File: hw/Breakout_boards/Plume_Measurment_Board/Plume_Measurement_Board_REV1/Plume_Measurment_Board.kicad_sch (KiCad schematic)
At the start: 34 parts, among them U2 LMP7721MA/NOPB, U3 LMP2022MA/NOPB, U4 AD8475ARMZ, U5 AD8475ARMZ, U7 AD7176-2BRUZ

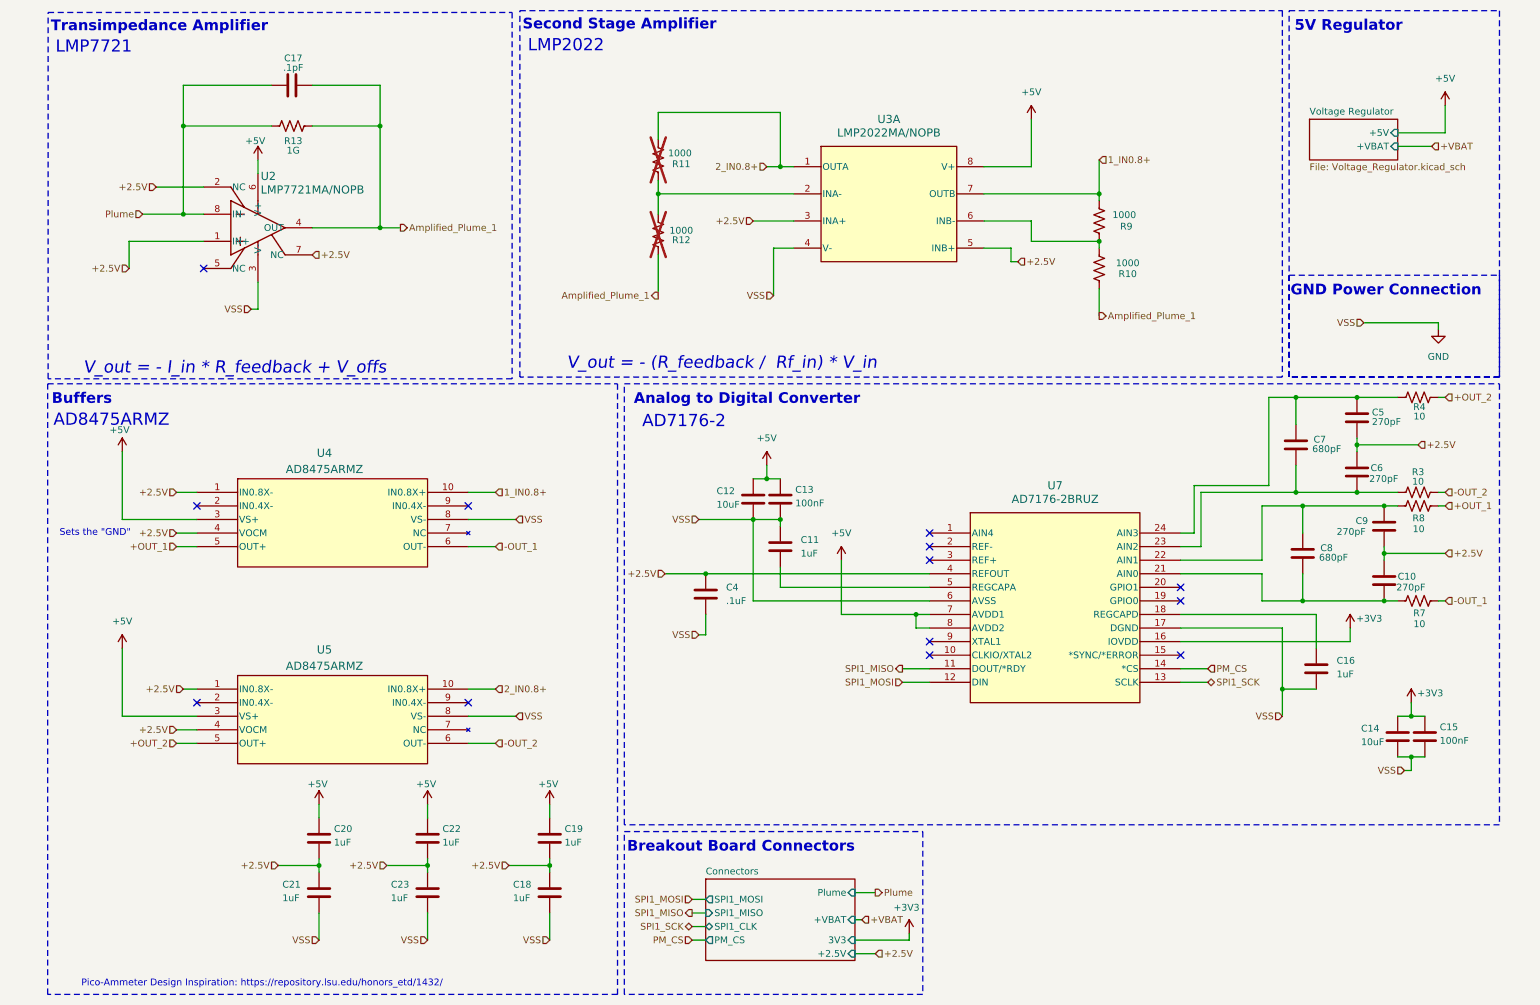
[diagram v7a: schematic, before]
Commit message: New Schematic w/ Addition of two E-spray Amplification Signals
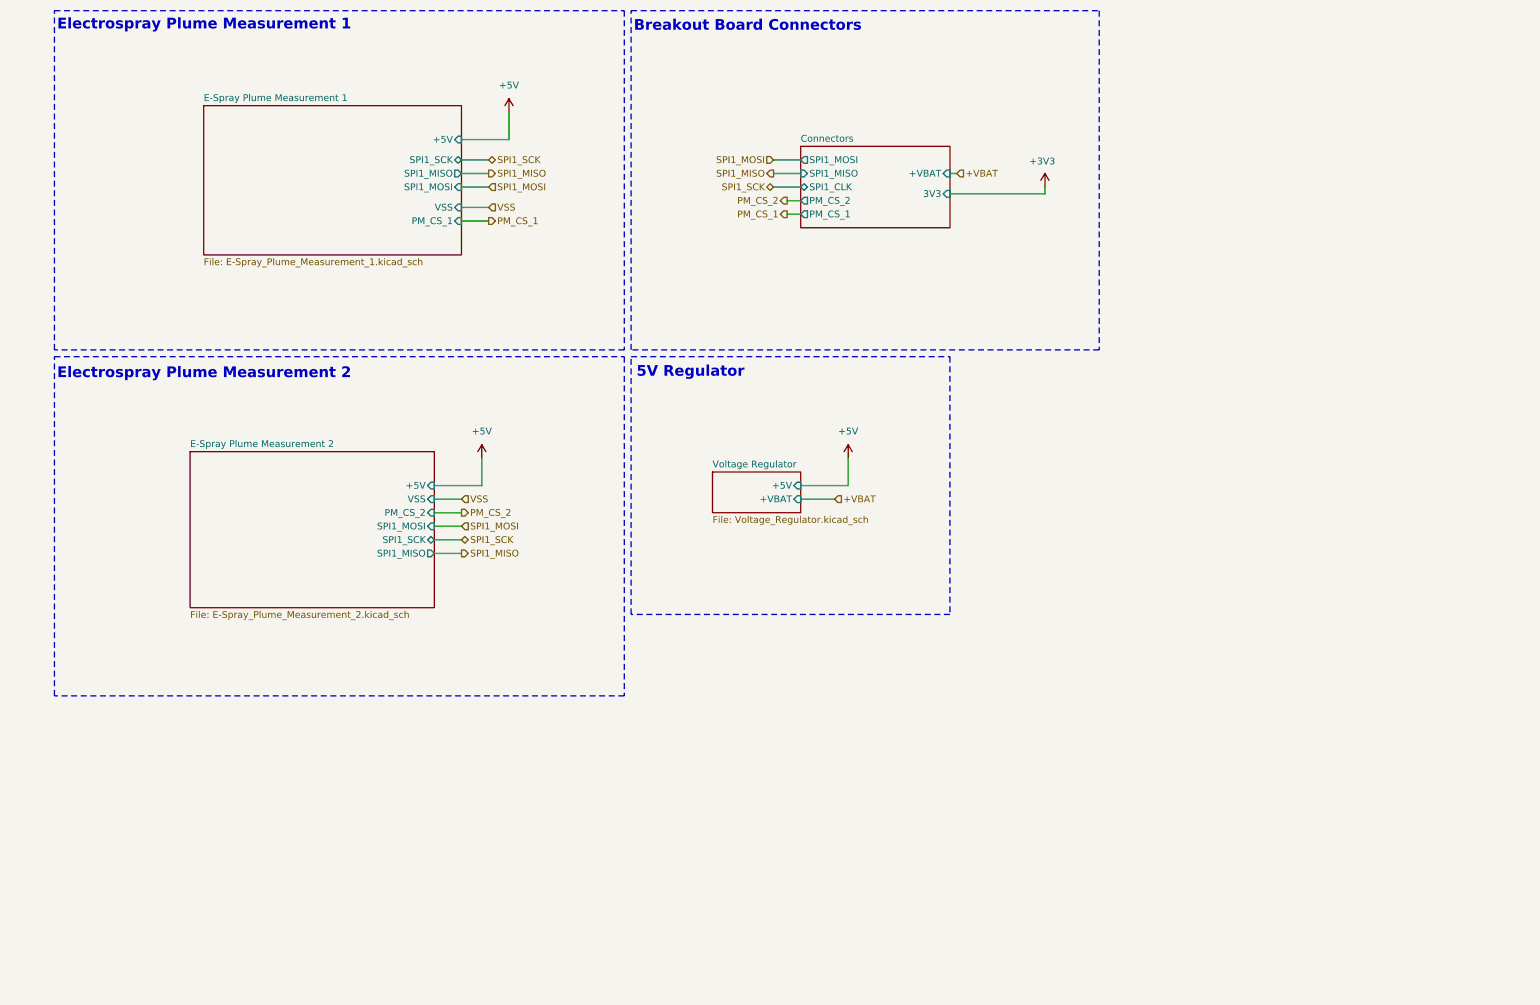
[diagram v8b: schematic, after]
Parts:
- removed C10, C5, C6, C9: 270pF, Capacitor_SMD:C_0603_1608Metric_Pad1.08x0.95mm_HandSolder, symbol Device:C
- removed C11, C19, C20, C22: 1uF, Capacitor_SMD:C_0603_1608Metric_Pad1.08x0.95mm_HandSolder, symbol Device:C
- removed C12, C14: 10uF, Capacitor_SMD:C_0805_2012Metric_Pad1.18x1.45mm_HandSolder, symbol Device:C
- removed C13, C15: 100nF, Capacitor_SMD:C_0603_1608Metric_Pad1.08x0.95mm_HandSolder, symbol Device:C
- removed C16, C18, C21, C23: 1uF, Capacitor_SMD:C_0805_2012Metric_Pad1.18x1.45mm_HandSolder, symbol Device:C
- removed C17: .1pF, Capacitor_SMD:C_0402_1005Metric_Pad0.74x0.62mm_HandSolder, symbol Device:C
- removed C4: .1uF, Capacitor_SMD:C_0603_1608Metric_Pad1.08x0.95mm_HandSolder, symbol Device:C
- removed C7, C8: 680pF, Capacitor_SMD:C_0603_1608Metric_Pad1.08x0.95mm_HandSolder, symbol Device:C
- removed R10, R11, R12, R9: 1000, Resistor_SMD:R_0603_1608Metric_Pad0.98x0.95mm_HandSolder, symbol Device:R_US
- removed R13: 1G, Resistor_SMD:R_2512_6332Metric_Pad1.40x3.35mm_HandSolder, symbol Device:R_US
- removed R3, R4, R7, R8: 10, Resistor_SMD:R_0603_1608Metric_Pad0.98x0.95mm_HandSolder, symbol Device:R_US
- removed U2: LMP7721MA/NOPB, Amplifier_Texas_Instruments:M08A, symbol Amplifier_Texas_Instruments:LMP7721MA_NOPB
- removed U3: LMP2022MA/NOPB, Amplifier_Texas_Instruments:M08A, symbol Amplifier_Texas_Instruments:LMP2022MA_NOPB
- removed U4, U5: AD8475ARMZ, Buffer_Analog_Devices:RM_10_ADI, symbol Amplifier_Buffer_Texas_Instruments:AD8475ARMZ
- removed U7: AD7176-2BRUZ, ADC_Analog_Devices:RU_24_ADI, symbol ADC_Analog_Devices:AD7176-2BRUZ
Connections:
- no-connect marks 13 -> 0
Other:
- added sheet E-Spray Plume Measurement 1 (E-Spray_Plume_Measurement_1.kicad_sch)
- added sheet E-Spray Plume Measurement 2 (E-Spray_Plume_Measurement_2.kicad_sch)
- sheet Connectors ports: added PM_CS_1, PM_CS_2; removed +2.5V, PM_CS, Plume
- note added: "Electrospray Plume Measurement 1"
- note added: "Electrospray Plume Measurement 2"
- note removed: "AD7176-2"
- note removed: "AD8475ARMZ"
- note removed: "Analog to Digital Converter"
- note removed: "Buffers"
- note removed: "GND Power Connection"
- note removed: "LMP2022"
- note removed: "LMP7721"
- note removed: "Pico-Ammeter Design Inspiration: https://repository.lsu.edu/honors_etd/1432/"
- note removed: "Second Stage Amplifier"
- note removed: "Sets the "GND""
- note removed: "Transimpedance Amplifier"
- note removed: "V_out = - (R_feedback / Rf_in) * V_in"
- note removed: "V_out = - I_in * R_feedback + V_offs"
